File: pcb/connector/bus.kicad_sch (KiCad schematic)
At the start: 2 parts, among them J201 Conn_01x05, J202 Conn_01x06

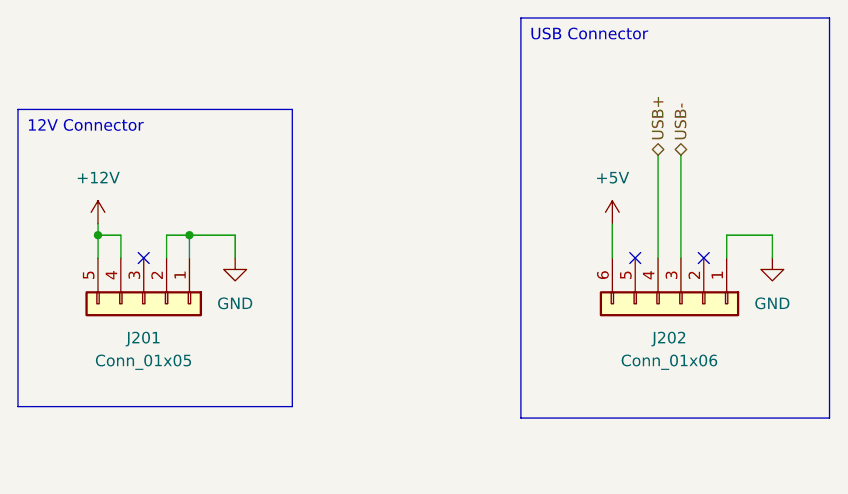
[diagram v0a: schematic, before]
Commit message: update bus schematic
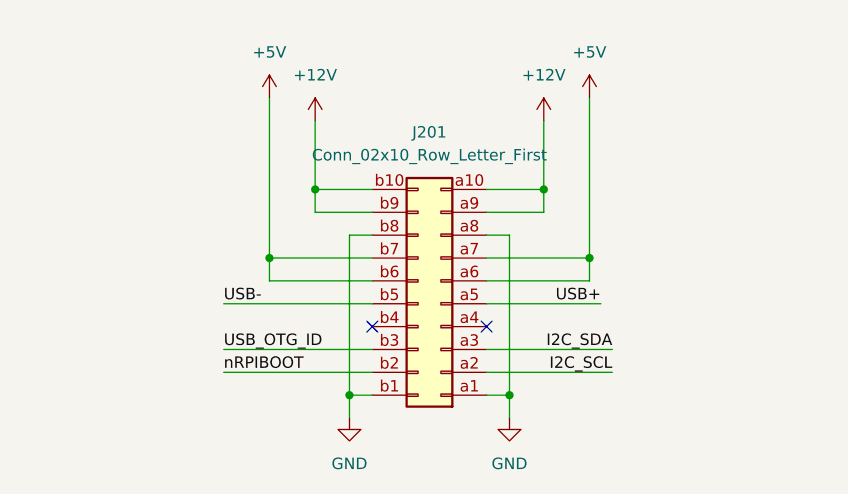
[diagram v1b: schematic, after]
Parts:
- removed J201: Conn_01x05, symbol Connector_Generic:Conn_01x05
- removed J202: Conn_01x06, symbol Connector_Generic:Conn_01x06
- added J201: Conn_02x10_Row_Letter_First, PRJ:PCN10-20P-2.54DS, symbol Connector_Generic:Conn_02x10_Row_Letter_First
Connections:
- net +12V: now also J201.a10 (Pin_a10), J201.a9 (Pin_a9), J201.b10 (Pin_b10), J201.b9 (Pin_b9)
- net +5V: now also J201.a6 (Pin_a6), J201.a7 (Pin_a7), J201.b6 (Pin_b6), J201.b7 (Pin_b7)
- net GND: now also J201.a1 (Pin_a1), J201.a8 (Pin_a8), J201.b1 (Pin_b1), J201.b8 (Pin_b8)
- net USB+: now also J201.a5 (Pin_a5)
- net USB-: now also J201.b5 (Pin_b5)
- new net I2C_SCL: J201.a2 (Pin_a2)
- new net I2C_SDA: J201.a3 (Pin_a3)
- new net USB_OTG_ID: J201.b3 (Pin_b3)
- new net nRPIBOOT: J201.b2 (Pin_b2)
- no-connect marks 3 -> 2
